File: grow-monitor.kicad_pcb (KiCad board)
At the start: 4 copper layers, 20 x 140 mm, 63 parts, among them J1 PH 2.0, J2 I2C1, J3 DS18B20, M1 M5StampS3, M2 AHT21B, Q1 AO3401A, Q2 ALS-PT19-315C, Q3 AO3401A, Q4 2N7002, SW1 PWR2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

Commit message: More improvements
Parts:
- removed TP11: TestPoint, TestPoint:TestPoint_Pad_1.0x1.0mm
- JP5, JP6, TP1, TP10, TP2, TP3, TP6, TP7, TP8, TP9: footprint TestPoint:TestPoint_Pad_1.0x1.0mm -> local:TestPoint_Pad_1.0x1.0mm
- moved TP3 24.3 mm to (66.0, 52.2)
- moved TP2 22.2 mm to (64.5, 53.5)
- moved JP6 19.0 mm to (55.5, 59.9)
- moved JP5 15.7 mm to (55.5, 62.5)
- moved TP1 14.6 mm to (66.0, 61.1)
- moved TP6 9.77 mm to (54.0, 63.7)
- moved R22 8.96 mm to (55.2, 82.5)
- moved TP7 8.04 mm to (54.0, 61.1)
- moved TP9 7.21 mm to (54.0, 56.0)
- moved TP10 6.00 mm to (54.0, 53.5)
- moved TP8 5.99 mm to (54.0, 58.6)
- moved R6 5.72 mm to (51.8, 88.0), turned to 180 degrees
- moved D5 5.00 mm to (59.3, 90.2)
- moved D4 5.00 mm to (62.9, 90.2)
- moved R5 2.34 mm to (51.8, 89.8)
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- renumbered TP5 to C7
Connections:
- RN1 pad 1: /CALIB -> Net-(D1-A)
- RN1 pad 2: Net-(D1-A) -> /CALIB
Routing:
- net /TH_PWR: track 0.00 -> 164.4 mm, vias 0 -> 3
- net /T_SENSE: track 0.00 -> 164.1 mm, vias 0 -> 3
- net GND: track 0.00 -> 128.4 mm, vias 0 -> 31
- net /EN: track 0.00 -> 52.0 mm, vias 0 -> 3
- net /S_SENSE: track 0.00 -> 50.9 mm, vias 0 -> 2
- net Net-(D3-A): track 0.00 -> 49.6 mm, vias 0 -> 2
- net /B_VOLT: track 0.00 -> 47.6 mm
- net /PWM: track 0.00 -> 47.5 mm, vias 0 -> 2
- net /CALIB: track 0.00 -> 43.7 mm, vias 0 -> 3
- net /PROG: track 0.00 -> 41.6 mm, vias 0 -> 3
- net /SCL: track 0.00 -> 37.9 mm, vias 0 -> 1
- net /DS18B20: track 0.00 -> 33.5 mm, vias 0 -> 1
- net /DONE: track 0.00 -> 30.8 mm, vias 0 -> 3
- net /SDA: track 0.00 -> 29.7 mm
- net +BATT: track 0.00 -> 27.8 mm, vias 0 -> 1
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- added copper zone on In2.Cu, net +3V3
- added copper zone on B.Cu, net GND
- added copper zone on F.Cu, net GND

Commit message: More tweaks
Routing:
- net /TH_PWR: track 164.4 -> 157.5 mm, vias 3 -> 4
- net /B_VOLT: track 47.6 -> 41.6 mm, vias 0 -> 3
- net /S_SENSE: track 50.9 -> 47.9 mm
- net GND: track 128.4 -> 130.9 mm
- net Net-(Q1-G): track 8.68 -> 7.41 mm
- net /T_SENSE: track 164.1 -> 165.0 mm
- net /EN: track 52.0 -> 51.2 mm
- net Net-(D3-A): track 49.6 -> 49.8 mm, vias 2 -> 1

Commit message: Switched jumpers to use stock cct by default
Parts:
- turned JP2 to 0 degrees
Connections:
- Q1 pad 3: Net-(JP2-B) -> Net-(JP2-A)
- Q3 pad 3: Net-(JP2-A) -> Net-(JP2-B)
- R22 pad 1: Net-(JP2-A) -> Net-(JP2-B)
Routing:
- net Net-(JP2-B): track 13.3 -> 27.5 mm, vias 2 -> 0
- net Net-(JP2-A): track 27.5 -> 13.3 mm, vias 0 -> 2

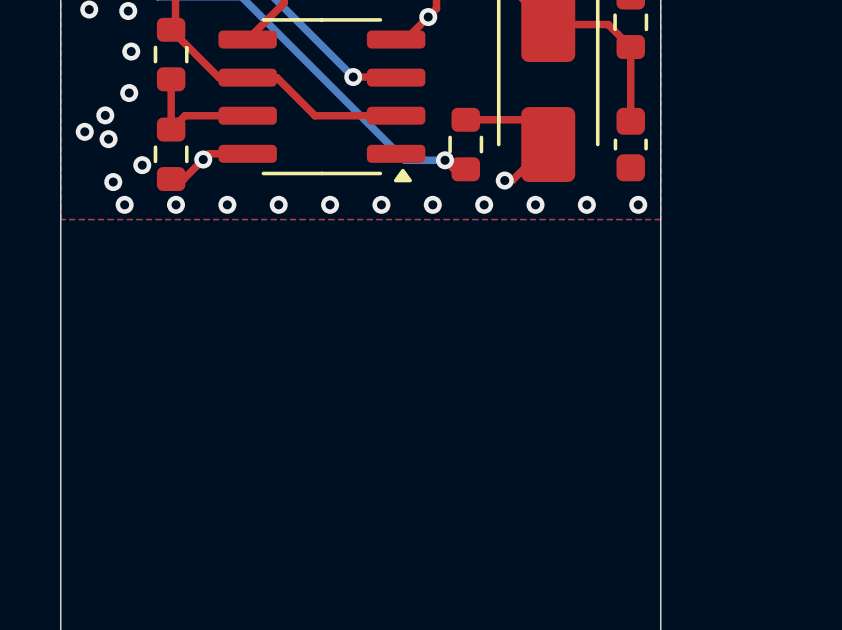
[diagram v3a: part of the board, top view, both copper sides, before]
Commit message: Added title, revision, email and date
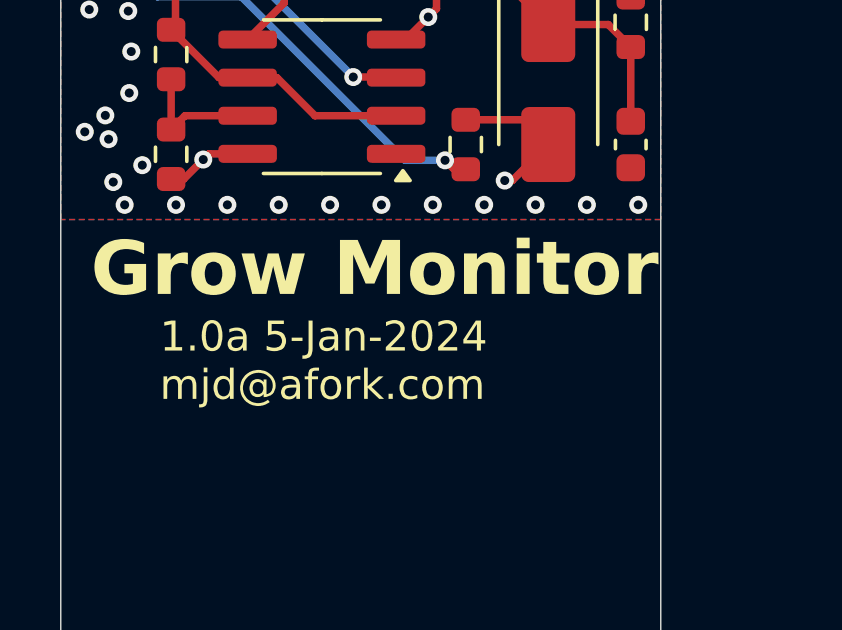
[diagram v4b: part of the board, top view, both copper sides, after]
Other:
- board text added: "${REVISION} ${ISSUE_DATE} ${COMPANY}"
- board text added: "Grow Monitor"
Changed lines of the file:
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@@
 	)
 	(paper "A4")
+	(title_block
+		(date "5-Jan-2024")
+		(rev "1.0a")
+		(company "mjd@afork.com")
+	)
 	(layers
 		(0 "F.Cu" signal)
@@
 		(tags "net tie solder jumper bridged")
 		(property "Reference" "JP2"
-			(at 0 1.8 360)
+			(at 0 1.8 0)
 			(layer "B.SilkS")
 			(hide yes)
@@
 		)
 		(property "Value" "PWR_SELECT"
-			(at 0 -2 360)
+			(at 0 -2 0)
 			(layer "B.Fab")
 			(effects
@@
 		(tags "net tie solder jumper bridged")
 		(property "Reference" "JP1"
-			(at 0 1.8 360)
+			(at 0 1.8 0)
 			(layer "B.SilkS")
 			(hide yes)
@@
 		)
 		(property "Value" "PWM_SELECT"
-			(at 0 -2 360)
+			(at 0 -2 0)
 			(layer "B.Fab")
 			(effects
@@
 			)
 			(justify left bottom)
+		)
+	)
+	(gr_text "${REVISION} ${ISSUE_DATE}\n${COMPANY}"
+		(at 53.3 107.1 0)
+		(layer "F.SilkS")
+		(effects
+			(font
+				(size 1 1)
+				(thickness 0.1)
+			)
+			(justify left bottom)
+		)
+	)
+	(gr_text "Grow Monitor"
+		(at 51 103.7 0)
+		(layer "F.SilkS")
+		(effects
+			(font
+				(size 1.8 1.8)
+				(thickness 0.3)
+				(bold yes)
+			)
+			(justify left bottom)

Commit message: Reimport from schematic
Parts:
- C3: value 22u -> 22u 25V
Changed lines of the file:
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@@
 			)
 		)
-		(property "Value" "22u"
+		(property "Value" "22u 25V"
 			(at 0 1.68 90)
 			(layer "F.Fab")
@@
 			)
 		)
-		(property "LCSC" ""
+		(property "LCSC" "C45783"
 			(at 0 0 270)
 			(unlocked yes)
